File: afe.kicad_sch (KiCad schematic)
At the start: 163 parts, among them J1 Conn_01x18, Q1 Q_NMOS_GDS, Q10 Q_NMOS_GDS, Q11 Q_NMOS_GDS, Q12 Q_NMOS_GDS, Q13 Q_NMOS_GDS, Q14 Q_NMOS_GDS, Q15 Q_NMOS_GDS, Q16 Q_NMOS_GDS, Q17 Q_NMOS_GDS, Q18 Q_NMOS_GDS, Q19 Q_NMOS_GDS, Q2 Q_NMOS_GDS, Q20 Q_NMOS_GDS, Q21 Q_NMOS_GDS, Q22 Q_NMOS_GDS, Q23 Q_NMOS_GDS, Q24 Q_NMOS_GDS, Q25 Q_NMOS_GDS, Q26 Q_NMOS_GDS, Q29 Q_NMOS_GDS, Q3 Q_PMOS_GDS, Q30 Q_NMOS_GDS, Q31 Q_NMOS_GDS, Q32 Q_NMOS_GDS, Q33 Q_NMOS_GDS, Q34 Q_NMOS_GDS, Q35 Q_NMOS_GDS, Q36 Q_NMOS_GDS, Q37 Q_NMOS_GDS, Q38 Q_NMOS_GDS, Q4 Q_NPN_BEC, U1 PB7170

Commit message: 分配封装，添加RS485通信接口，调整布局，传感器连接到独立MCU上
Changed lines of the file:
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@@
-		)
-	)
-	(label "MISO"
-		(at 71.12 97.79 180)
-		(effects
-			(font
-				(size 1.27 1.27)
-			)
-			(justify right bottom)
 		)
 	)
@@
 		)
 	)
-	(label "CS_AFE"
-		(at 71.12 102.87 180)
-		(effects
-			(font
-				(size 1.27 1.27)
-			)
-			(justify right bottom)
-		)
-	)
 	(label "S4"
 		(at 115.57 128.27 0)
@@
 		)
 	)
-	(label "SCLK"
-		(at 71.12 105.41 180)
-		(effects
-			(font
-				(size 1.27 1.27)
-			)
-			(justify right bottom)
-		)
-	)
 	(label "DSG"
 		(at 53.34 147.32 180)
@@
 		)
 	)
-	(label "GPIO2"
-		(at 71.12 95.25 180)
-		(effects
-			(font
-				(size 1.27 1.27)
-			)
-			(justify right bottom)
-		)
-	)
 	(label "SRN"
 		(at 86.36 146.05 180)
@@
 		)
 	)
-	(label "MOSI"
-		(at 71.12 100.33 180)
-		(effects
-			(font
-				(size 1.27 1.27)
-			)
-			(justify right bottom)
-		)
-	)
 	(label "S10"
 		(at 115.57 97.79 0)
@@
 		)
 	)
-	(label "GPIO1"
-		(at 71.12 92.71 180)
-		(effects
-			(font
-				(size 1.27 1.27)
-			)
-			(justify right bottom)
-		)
-	)
 	(label "SW_MID"
 		(at 66.04 167.64 90)
@@
 		)
 	)
+	(hierarchical_label "MOSI"
+		(shape input)
+		(at 71.12 100.33 180)
+		(effects
+			(font
+				(size 1.27 1.27)
+			)
+			(justify right)
+		)
+	)
+	(hierarchical_label "GPIO1"
+		(shape bidirectional)
+		(at 71.12 92.71 180)
+		(effects
+			(font
+				(size 1.27 1.27)
+			)
+			(justify right)
+		)
+	)
+	(hierarchical_label "GPIO2"
+		(shape bidirectional)
+		(at 71.12 95.25 180)
+		(effects
+			(font
+				(size 1.27 1.27)
+			)
+			(justify right)
+		)
+	)
+	(hierarchical_label "SCLK"
+		(shape input)
+		(at 71.12 105.41 180)
+		(effects
+			(font
+				(size 1.27 1.27)
+			)
+			(justify right)
+		)
+	)
+	(hierarchical_label "MISO"
+		(shape output)
+		(at 71.12 97.79 180)
+		(effects
+			(font
+				(size 1.27 1.27)
+			)
+			(justify right)
+		)
+	)
+	(hierarchical_label "CS_AFE"
+		(shape input)
+		(at 71.12 102.87 180)
+		(effects
+			(font
+				(size 1.27 1.27)
+			)
+			(justify right)
+		)
+	)

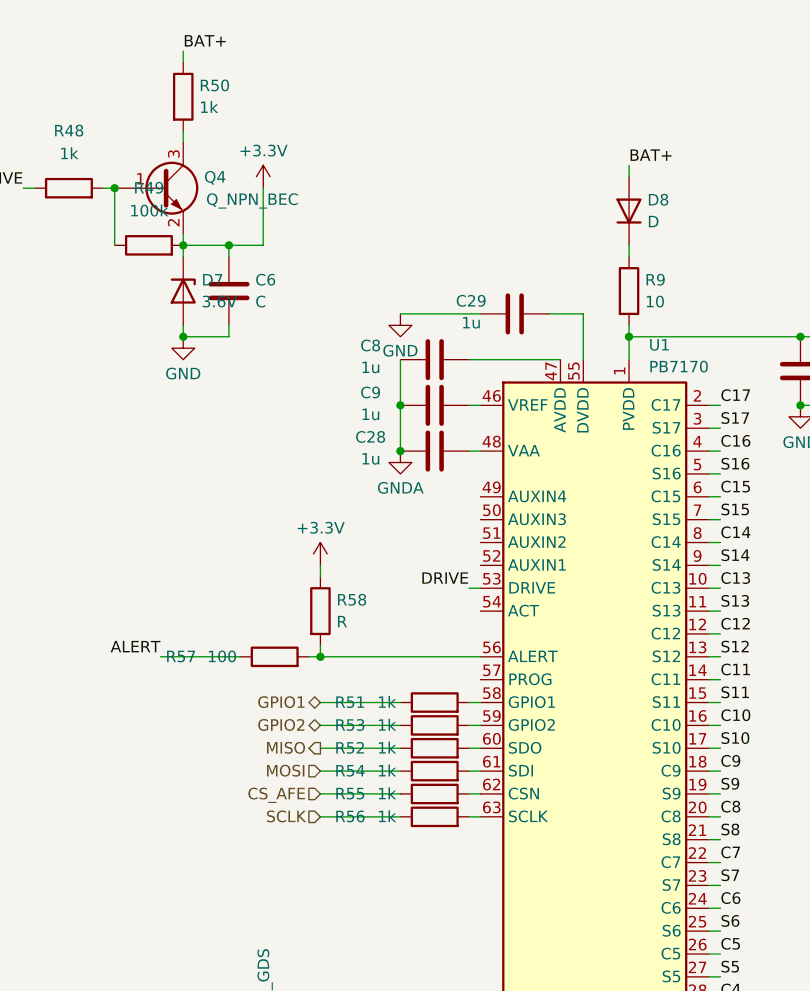
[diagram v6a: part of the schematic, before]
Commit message: 修改电源电路
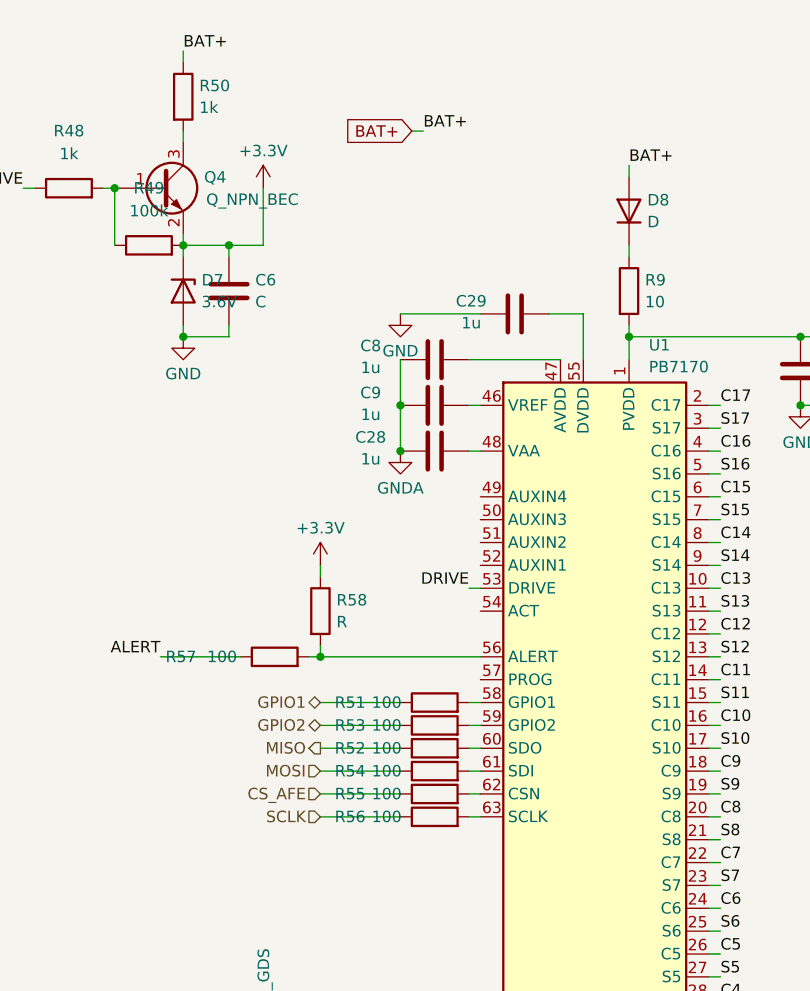
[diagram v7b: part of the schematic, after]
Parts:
- R51, R52, R53, R54, R55, R56: value 1k -> 100
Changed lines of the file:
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@@
 	(wire
 		(pts
+			(xy 81.28 29.21) (xy 82.55 29.21)
+		)
+		(stroke
+			(width 0)
+			(type default)
+		)
+	)
+	(wire
+		(pts
 			(xy 203.2 132.08) (xy 212.09 132.08)
 		)
@@
 		)
 	)
+	(label "BAT+"
+		(at 82.55 29.21 0)
+		(effects
+			(font
+				(size 1.27 1.27)
+			)
+			(justify left bottom)
+		)
+	)
 	(label "C17"
 		(at 139.7 102.87 180)
@@
 		)
 	)
+	(global_label "BAT+"
+		(shape input)
+		(at 81.28 29.21 180)
+		(fields_autoplaced yes)
+		(effects
+			(font
+				(size 1.27 1.27)
+			)
+			(justify right)
+		)
+		(property "Intersheetrefs" "${INTERSHEET_REFS}"
+			(at 73.3962 29.21 0)
+			(effects
+				(font
+					(size 1.27 1.27)
+				)
+				(justify right)
+				(hide yes)
+			)
+		)
+	)
 	(hierarchical_label "MOSI"
 		(shape input)
@@
 			)
 		)
-		(property "Value" "1k"
+		(property "Value" "100"
 			(at 78.486 100.33 90)
 			(effects
@@
 			)
 		)
-		(property "Value" "1k"
+		(property "Value" "100"
 			(at 78.486 95.25 90)
 			(effects
@@
 			)
 		)
-		(property "Value" "1k"
+		(property "Value" "100"
 			(at 78.486 97.79 90)
 			(effects
@@
 			)
 		)
-		(property "Value" "1k"
+		(property "Value" "100"
 			(at 78.486 105.41 90)
 			(effects
@@
 			)
 		)
-		(property "Value" "1k"
+		(property "Value" "100"
 			(at 78.486 92.71 90)
 			(effects
@@
 			)
 		)
-		(property "Value" "1k"
+		(property "Value" "100"
 			(at 78.486 102.87 90)
 			(effects
